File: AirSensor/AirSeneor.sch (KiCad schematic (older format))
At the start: 39 parts, among them J1 EXT_ADC, J2 SWD, J3 UART, J4 M04x2, U1 SPX3819M5-L-3-3, U2 MS5611, U3 LMV324, U4 MS4525DO, U5 TJA1050, U6 STM32F072CBTx, Y1 8MHz

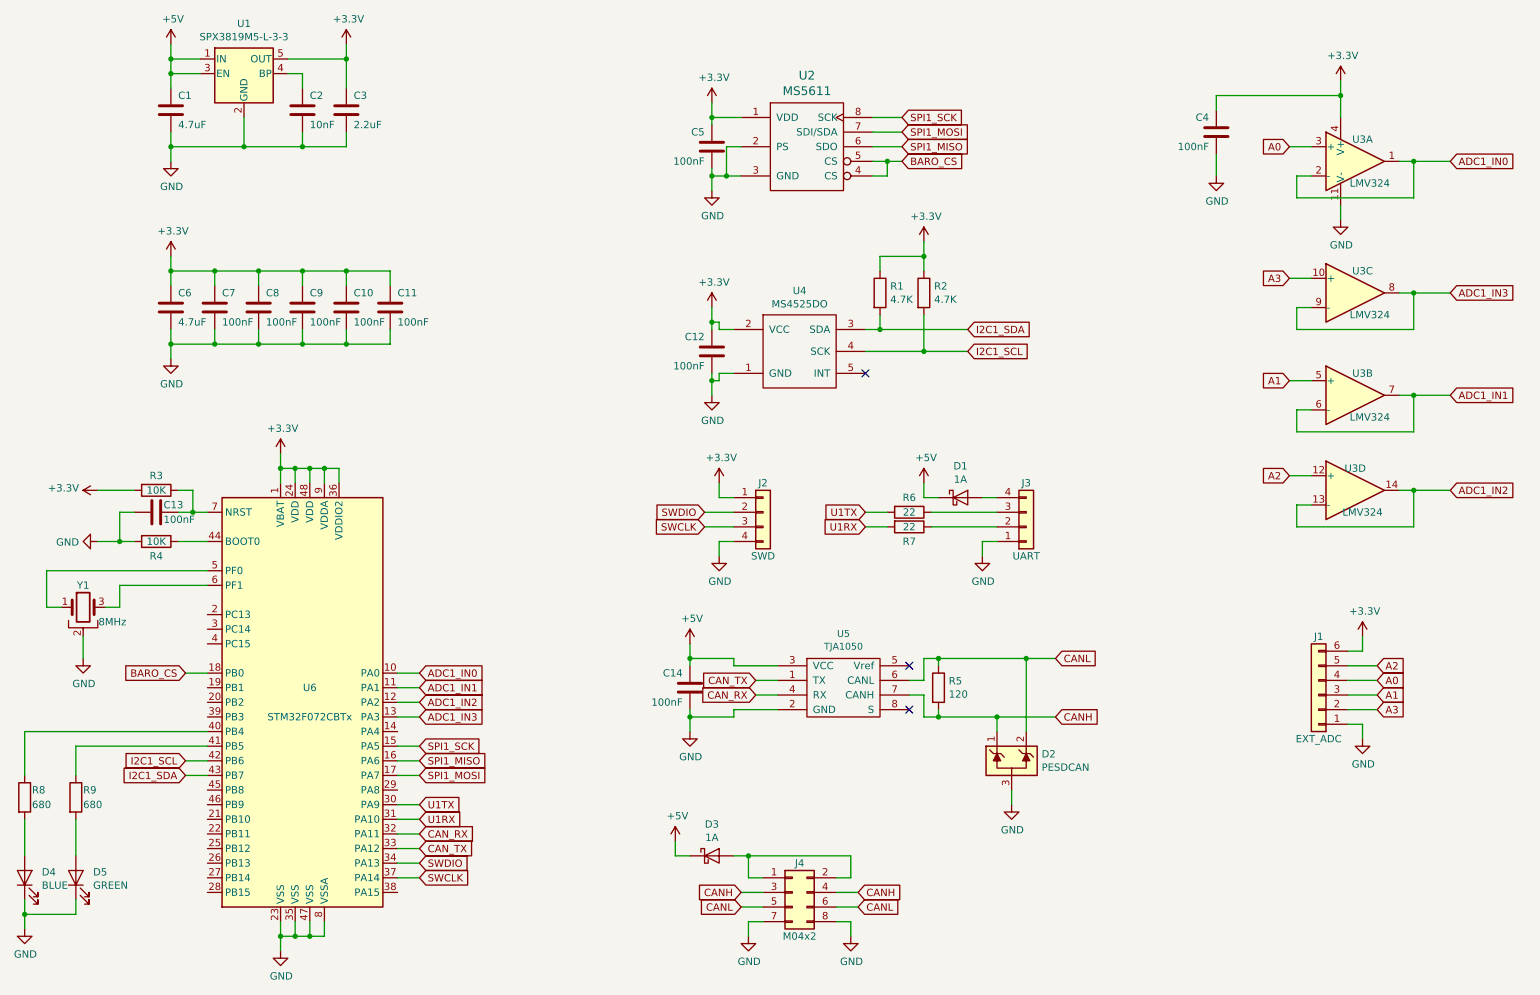
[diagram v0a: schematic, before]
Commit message: 1. Replace SWD connector with 10 pin SMD 2x5 connector in AirSensor. 2. Add signal name silk screen in AirSensor.
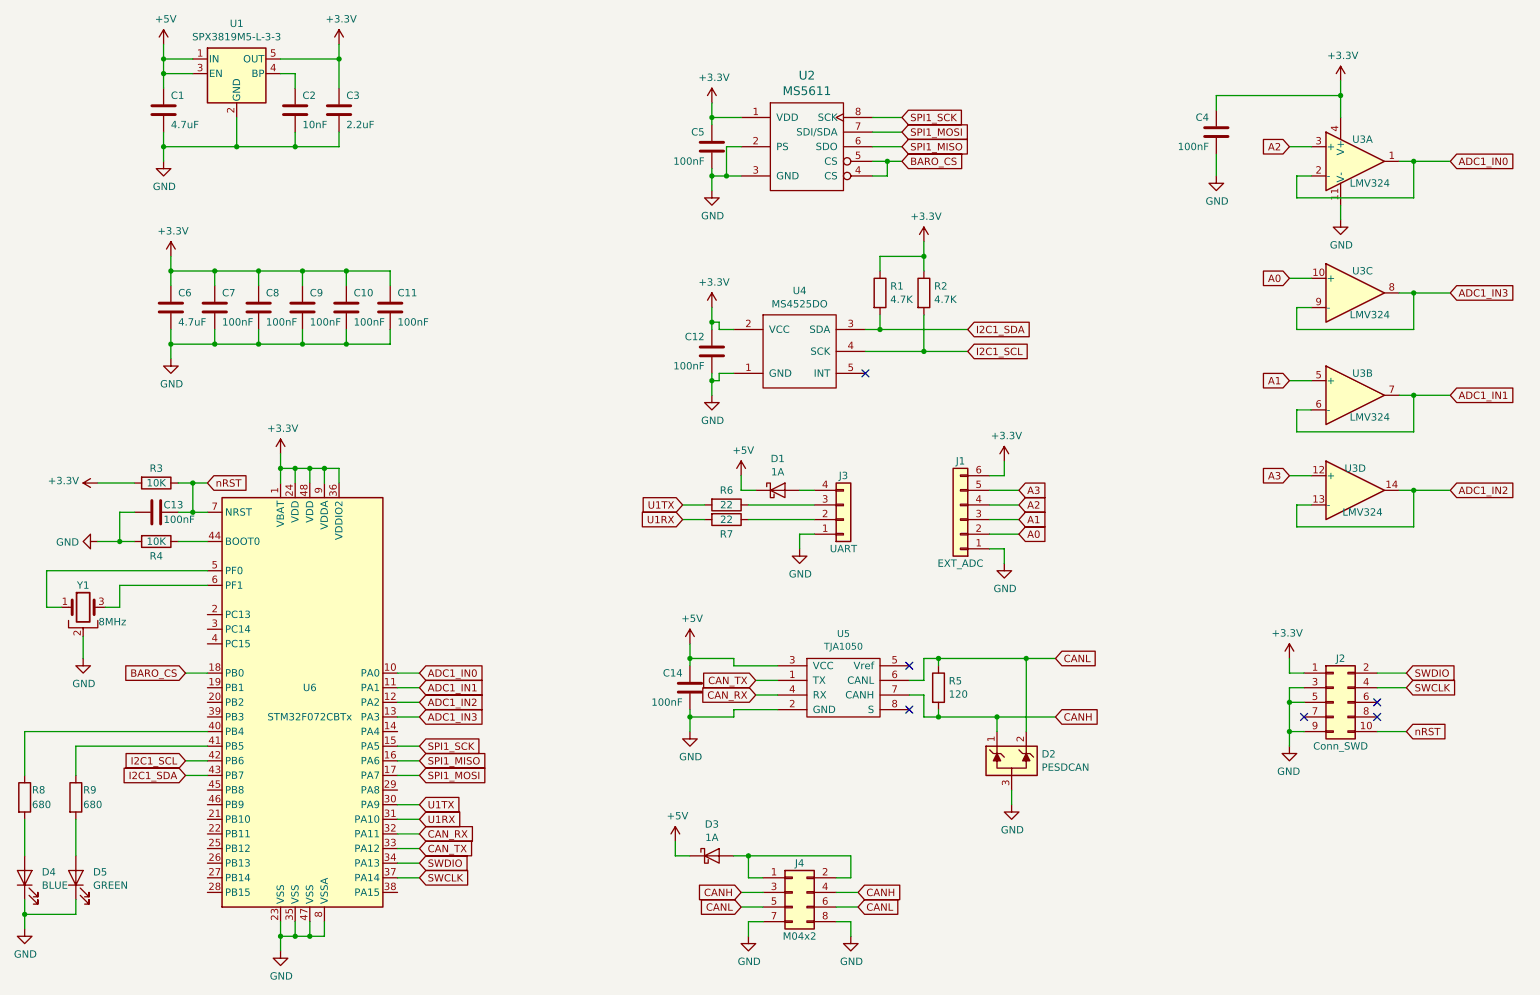
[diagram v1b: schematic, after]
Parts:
- removed J2: SWD, Connector_Molex:Molex_PicoBlade_53398-0471_1x04-1MP_P1.25mm_Vertical, symbol Connector_Generic:Conn_01x04
- added J2: Conn_SWD, Connector_PinHeader_1.27mm:PinHeader_2x05_P1.27mm_Vertical_SMD, symbol Connector_Generic:Conn_02x05_Odd_Even
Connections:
- net +3V3: now also J2.1 (Pin_1)
- net A0: now also J1.2 (Pin_2), U3.10 (+); no longer J1.4 (Pin_4), U3.3 (+)
- net A2: now also J1.4 (Pin_4), U3.3 (+); no longer J1.5 (Pin_5), U3.12 (+)
- net A3: now also J1.5 (Pin_5), U3.12 (+); no longer J1.2 (Pin_2), U3.10 (+)
- net GND: now also J2.3 (Pin_3), J2.5 (Pin_5), J2.9 (Pin_9)
- net SWCLK: now also J2.4 (Pin_4)
- net SWDIO: now also J2.2 (Pin_2)
- net nRST: now reaches C13.1, R3.1, U6.7 (NRST)
- net nRST: now also J2.10 (Pin_10)
- no-connect marks 3 -> 6
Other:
- moved on the sheet: C1, C2, C3, D1, J1, J3, R3, R6, R7, U1
